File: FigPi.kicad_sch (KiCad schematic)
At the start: 34 parts, among them J1 MOLEX_47346-100147346, J2 Debug, J3 PMW3/PMW4, J4 I2C1/PMW1, J5 SPI0/PWM2/PWM3, J6 I2C0/PMW0, J7 ADC/UART0/UART0/UART1/PWM5/PW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, SW1 KMS233GLFG, SW2 KMS233GLFG, U1 RP2040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

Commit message: Connected USBOOT properly to Boot button.  Had to move capacitor for new track.
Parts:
- U2: value QSPI NOR FLASH 2MiB 2x3mm USON (W25Q16JVUXIM) -> QSPI NOR FLASH 2MiB 2x3mm USON (W25Q16JVUXIQ)
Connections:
- net ~{USB_BOOT}: now also U1.31 (GPIO20)
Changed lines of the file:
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@@
+    (stroke (width 0) (type default) (color 0 0 0 0))
+  )
+  (wire (pts (xy 125.73 213.36) (xy 133.35 213.36))
     (stroke (width 0) (type default) (color 0 0 0 0))
   )
@@
   )
   (label "LED_G" (at 175.26 93.98 0)
+    (effects (font (size 1.27 1.27)) (justify left bottom))
+  )
+  (label "~{USB_BOOT}" (at 127 213.36 0)
     (effects (font (size 1.27 1.27)) (justify left bottom))
   )
@@
       (effects (font (size 1.4986 1.4986)) (justify left bottom))
     )
-    (property "Value" "QSPI NOR FLASH 2MiB 2x3mm USON (W25Q16JVUXIM)" (id 1) (at 227.33 82.55 0)
+    (property "Value" "QSPI NOR FLASH 2MiB 2x3mm USON (W25Q16JVUXIQ)" (id 1) (at 227.33 82.55 0)
       (effects (font (size 1.4986 1.4986)) (justify left bottom))
     )
@@
     )
     (path "/00000000-0000-0000-0000-0000bf9d4e19"
-      (reference "U2") (unit 1) (value "QSPI NOR FLASH 2MiB 2x3mm USON (W25Q16JVUXIM)") (footprint "USON8 2x3")
+      (reference "U2") (unit 1) (value "QSPI NOR FLASH 2MiB 2x3mm USON (W25Q16JVUXIQ)") (footprint "USON8 2x3")
     )
     (path "/c33e8e0a-d848-4eb4-9491-17734fe4442c"

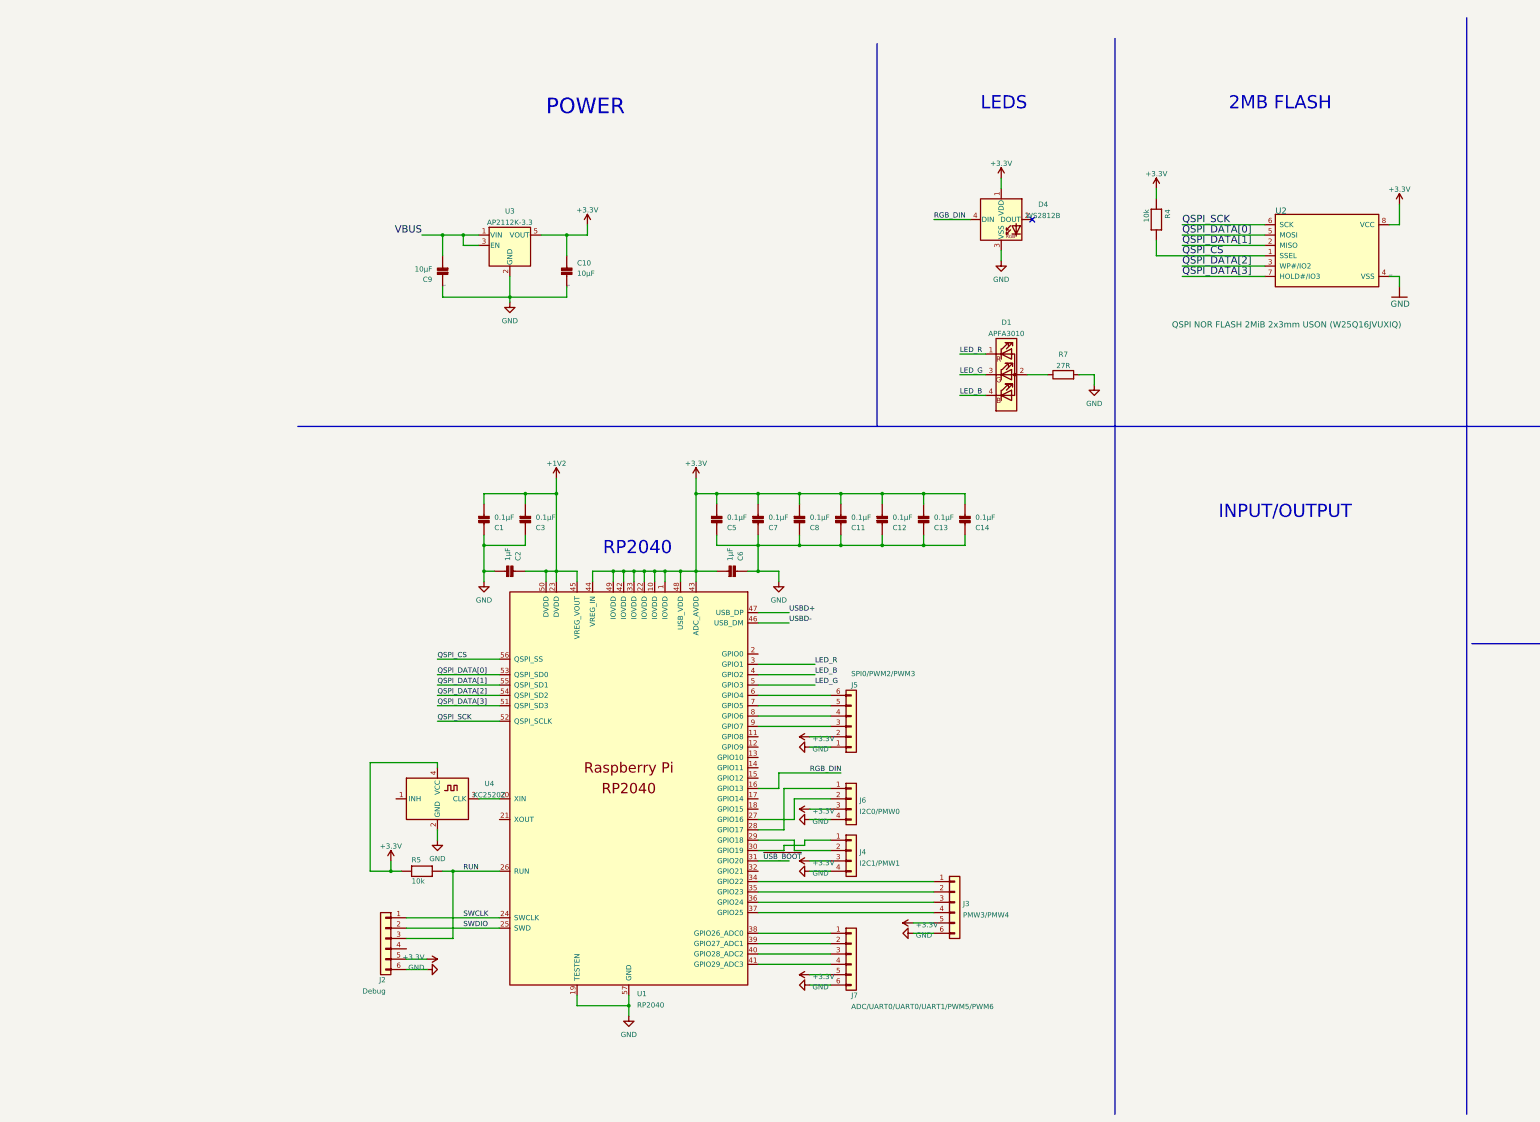
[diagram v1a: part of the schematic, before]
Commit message: v1.5 - Changed all JST connections to 4-pin.  Added 8 additional APA102 - 2020 LEDs for a 3 x 3 matrix.  Rearranged items as needed.  Moved SWDIO and SWCLK from JST connector to test pads.
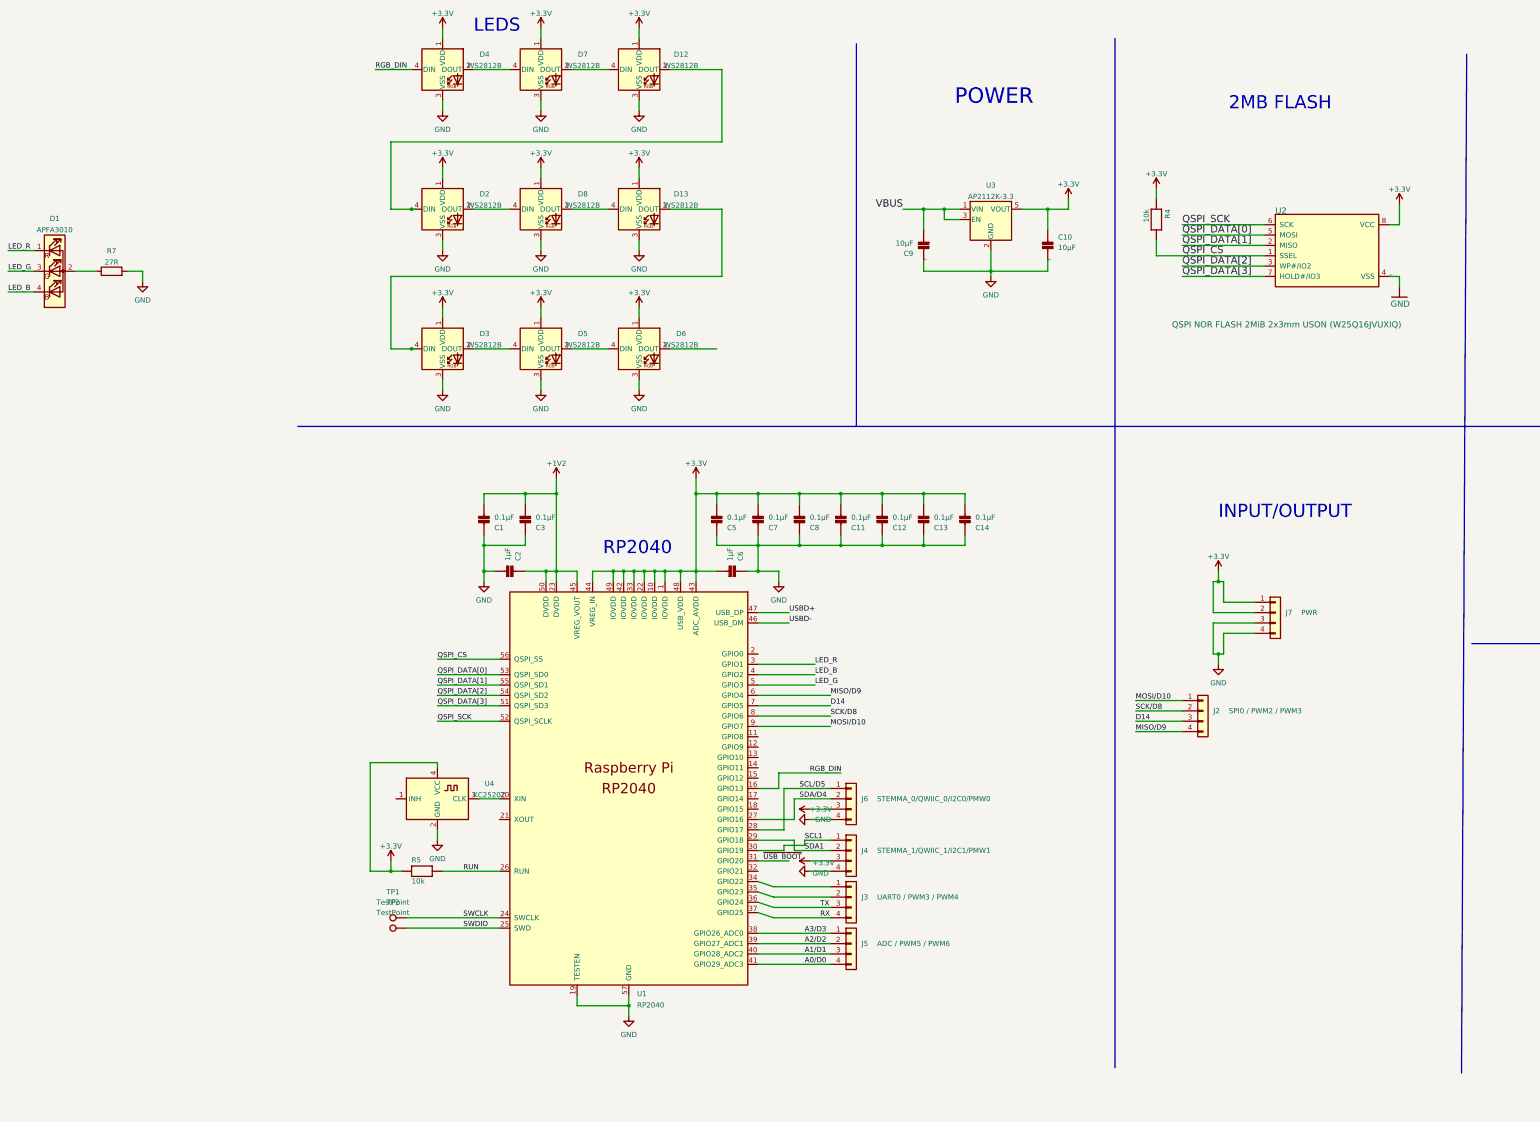
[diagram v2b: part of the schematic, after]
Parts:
- removed J2: Debug, Connector_JST:JST_SH_SM06B-SRSS-TB_1x06-1MP_P1.00mm_Horizontal, symbol Connector_Generic:Conn_01x06
- removed J3: PMW3/PMW4, Connector_JST:JST_SH_SM06B-SRSS-TB_1x06-1MP_P1.00mm_Horizontal, symbol Connector_Generic:Conn_01x06
- removed J5: SPI0/PWM2/PWM3, Connector_JST:JST_SH_SM06B-SRSS-TB_1x06-1MP_P1.00mm_Horizontal, symbol Connector_Generic:Conn_01x06
- removed J7: ADC/UART0/UART0/UART1/PWM5/PWM6, Connector_JST:JST_SH_SM06B-SRSS-TB_1x06-1MP_P1.00mm_Horizontal, symbol Connector_Generic:Conn_01x06
- added D12, D13, D2, D3, D5, D6, D7, D8: WS2812B, LED_SMD:LED_SK6812_EC15_1.5x1.5mm, symbol LED:WS2812B
- added J2: SPI0 / PWM2 / PWM3, Connector_JST:JST_SH_SM04B-SRSS-TB_1x04-1MP_P1.00mm_Horizontal, symbol Connector_Generic:Conn_01x04
- added J3: UART0 / PWM3 / PWM4, Connector_JST:JST_SH_SM04B-SRSS-TB_1x04-1MP_P1.00mm_Horizontal, symbol Connector_Generic:Conn_01x04
- added J5: ADC / PWM5 / PWM6, Connector_JST:JST_SH_SM04B-SRSS-TB_1x04-1MP_P1.00mm_Horizontal, symbol Connector_Generic:Conn_01x04
- added J7: PWR, Connector_JST:JST_SH_SM04B-SRSS-TB_1x04-1MP_P1.00mm_Horizontal, symbol Connector_Generic:Conn_01x04
- added TP1, TP2: TestPoint, TestPoint:TestPoint_Pad_D2.0mm, symbol Connector:TestPoint
- J4: value I2C1/PMW1 -> STEMMA_1/QWIIC_1/I2C1/PMW1
- J6: value I2C0/PMW0 -> STEMMA_0/QWIIC_0/I2C0/PMW0
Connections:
- net +3V3: now also D12.1 (VDD), D13.1 (VDD), D2.1 (VDD), D3.1 (VDD), D5.1 (VDD), D6.1 (VDD), D7.1 (VDD), D8.1 (VDD), J7.1 (Pin_1), J7.2 (Pin_2)
- net GND: now also D12.3 (VSS), D13.3 (VSS), D2.3 (VSS), D3.3 (VSS), D5.3 (VSS), D6.3 (VSS), D7.3 (VSS), D8.3 (VSS), J7.3 (Pin_3), J7.4 (Pin_4)
- net SWCLK: now also TP1.1
- net SWDIO: now also TP2.1
- net at U1.34 (GPIO22): now also J3.1 (Pin_1)
- net at U1.35 (GPIO23): now also J3.2 (Pin_2)
- net TX: now reaches U1.36 (GPIO24)
- net TX: now also J3.3 (Pin_3)
- net RX: now reaches U1.37 (GPIO25)
- net RX: now also J3.4 (Pin_4)
- net A3/D3: now reaches U1.38 (GPIO26_ADC0)
- net A3/D3: now also J5.1 (Pin_1)
- net A2/D2: now reaches U1.39 (GPIO27_ADC1)
- net A2/D2: now also J5.2 (Pin_2)
- net A1/D1: now reaches U1.40 (GPIO28_ADC2)
- net A1/D1: now also J5.3 (Pin_3)
- net A0/D0: now reaches U1.41 (GPIO29_ADC3)
- net A0/D0: now also J5.4 (Pin_4)
- net SCL/D5: now reaches J6.1 (Pin_1), U1.28 (GPIO17)
- net SDA/D4: now reaches J6.2 (Pin_2), U1.27 (GPIO16)
- net at D4.2 (DOUT): now also D7.4 (DIN)
- net MOSI/D10: now reaches U1.9 (GPIO7)
- net MOSI/D10: now also J2.1 (Pin_1)
- net SCK/D8: now reaches U1.8 (GPIO6)
- net SCK/D8: now also J2.2 (Pin_2)
- net D14: now reaches U1.7 (GPIO5)
- net D14: now also J2.3 (Pin_3)
- net MISO/D9: now reaches U1.6 (GPIO4)
- net MISO/D9: now also J2.4 (Pin_4)
- net SCL1: now reaches J4.1 (Pin_1), U1.30 (GPIO19)
- net SDA1: now reaches J4.2 (Pin_2), U1.29 (GPIO18)
- new net: D12.4 (DIN), D7.2 (DOUT)
- new net: D12.2 (DOUT), D2.4 (DIN)
- new net: D3.2 (DOUT), D5.4 (DIN)
- new net: D13.2 (DOUT), D3.4 (DIN)
- new net: D2.2 (DOUT), D8.4 (DIN)
- new net: D5.2 (DOUT), D6.4 (DIN)
- new net: D13.4 (DIN), D8.2 (DOUT)
- no-connect marks 2 -> 1
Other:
- moved on the sheet: C10, C9, D1, D4, R7, U3

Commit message: 1.6 - Minor Cosmetic Changes
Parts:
- TP1, TP2: footprint TestPoint:TestPoint_Pad_D2.0mm -> TestPoint:TestPoint_Pad_D1.0mm
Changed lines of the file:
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@@
     (property "Reference" "TP1" (id 0) (at 36.068 220.98 90))
     (property "Value" "TestPoint" (id 1) (at 36.068 223.52 90))
-    (property "Footprint" "TestPoint:TestPoint_Pad_D2.0mm" (id 2) (at 39.37 222.25 0)
+    (property "Footprint" "TestPoint:TestPoint_Pad_D1.0mm" (id 2) (at 39.37 222.25 0)
       (effects (font (size 1.27 1.27)) hide)
     )
@@
     (property "Reference" "TP2" (id 0) (at 36.068 223.52 90))
     (property "Value" "TestPoint" (id 1) (at 36.068 226.06 90))
-    (property "Footprint" "TestPoint:TestPoint_Pad_D2.0mm" (id 2) (at 39.37 224.79 0)
+    (property "Footprint" "TestPoint:TestPoint_Pad_D1.0mm" (id 2) (at 39.37 224.79 0)
       (effects (font (size 1.27 1.27)) hide)
     )
@@
     )
     (path "/8337b7f2-9099-4db8-9f9b-0f8820b9d737"
-      (reference "TP1") (unit 1) (value "TestPoint") (footprint "TestPoint:TestPoint_Pad_D2.0mm")
+      (reference "TP1") (unit 1) (value "TestPoint") (footprint "TestPoint:TestPoint_Pad_D1.0mm")
     )
     (path "/bf6723a1-f7a8-4f2e-8937-15d1f9150ef9"
-      (reference "TP2") (unit 1) (value "TestPoint") (footprint "TestPoint:TestPoint_Pad_D2.0mm")
+      (reference "TP2") (unit 1) (value "TestPoint") (footprint "TestPoint:TestPoint_Pad_D1.0mm")
     )
     (path "/8642366e-14d5-4a4a-acc5-de8c0e7dc7d5"

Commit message: Updated to Rev 2.1 - layout changes, smd size changes.
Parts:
- removed D1: APFA3010, LED_SMD:LED_Kingbright_APFA3010_3x1.5mm_Horizontal, symbol LED:APFA3010
- added D1: R6C-AM2N2LY, Custom_Library:LED_1.1x1.7mm, symbol Custom_Library:R6C-AM2N2LY
- C1, C11, C12, C13, C14, C3, C5, C6, C7, C8: footprint Capacitor_SMD:C_0603_1608Metric -> Capacitor_SMD:C_0402_1005Metric
- D10: renamed from D6; value WS2812B -> SK6805; footprint LED_SMD:LED_SK6812_EC15_1.5x1.5mm -> Custom_Library:LED_SK6805_EC15_1.5x1.5mm; symbol LED:WS2812B -> Custom_Library:SK6805
- D2: renamed from D4; value WS2812B -> SK6805; footprint LED_SMD:LED_SK6812_EC15_1.5x1.5mm -> Custom_Library:LED_SK6805_EC15_1.5x1.5mm; symbol LED:WS2812B -> Custom_Library:SK6805
- D3: renamed from D2; value WS2812B -> SK6805; footprint LED_SMD:LED_SK6812_EC15_1.5x1.5mm -> Custom_Library:LED_SK6805_EC15_1.5x1.5mm; symbol LED:WS2812B -> Custom_Library:SK6805
- D4: renamed from D3; value WS2812B -> SK6805; footprint LED_SMD:LED_SK6812_EC15_1.5x1.5mm -> Custom_Library:LED_SK6805_EC15_1.5x1.5mm; symbol LED:WS2812B -> Custom_Library:SK6805
- D5: renamed from D7; value WS2812B -> SK6805; footprint LED_SMD:LED_SK6812_EC15_1.5x1.5mm -> Custom_Library:LED_SK6805_EC15_1.5x1.5mm; symbol LED:WS2812B -> Custom_Library:SK6805
- D6: renamed from D8; value WS2812B -> SK6805; footprint LED_SMD:LED_SK6812_EC15_1.5x1.5mm -> Custom_Library:LED_SK6805_EC15_1.5x1.5mm; symbol LED:WS2812B -> Custom_Library:SK6805
- D7: renamed from D5; value WS2812B -> SK6805; footprint LED_SMD:LED_SK6812_EC15_1.5x1.5mm -> Custom_Library:LED_SK6805_EC15_1.5x1.5mm; symbol LED:WS2812B -> Custom_Library:SK6805
- D8: renamed from D12; value WS2812B -> SK6805; footprint LED_SMD:LED_SK6812_EC15_1.5x1.5mm -> Custom_Library:LED_SK6805_EC15_1.5x1.5mm; symbol LED:WS2812B -> Custom_Library:SK6805
- D9: renamed from D13; value WS2812B -> SK6805; footprint LED_SMD:LED_SK6812_EC15_1.5x1.5mm -> Custom_Library:LED_SK6805_EC15_1.5x1.5mm; symbol LED:WS2812B -> Custom_Library:SK6805
- R1, R2: value 27Ω -> 27.4Ω; footprint Resistor_SMD:R_0603_1608Metric -> Resistor_SMD:R_0402_1005Metric
- R3, R4, R5: footprint Resistor_SMD:R_0603_1608Metric -> Resistor_SMD:R_0402_1005Metric
- R7: value 27R -> 260R
- U2: footprint USON8 2x3 -> Custom_Library:USON-8_L3.0-W2.0-P0.50-BL-EP
- U4: value KC2520Z -> OT201612MJBA4SL; footprint Oscillator:Oscillator_SMD_Kyocera_KC2520Z-4Pin_2.5x2.0mm -> Custom_Library:Oscillator_SMD_Yangzing_Tech_SMD2016-4P; JLCPCB P/N (none) -> C669076
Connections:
- net +3V3: now also D10.2 (VDD), D2.2 (VDD), D3.2 (VDD), D4.2 (VDD), D5.2 (VDD), D6.2 (VDD), D7.2 (VDD), D8.2 (VDD), D9.2 (VDD); no longer D10.1 (VDD), D2.1 (VDD), D3.1 (VDD), D4.1 (VDD), D5.1 (VDD), D6.1 (VDD), D7.1 (VDD), D8.1 (VDD), D9.1 (VDD)
- net GND: now also D10.4 (VSS), D2.4 (VSS), D3.4 (VSS), D4.4 (VSS), D5.4 (VSS), D6.4 (VSS), D7.4 (VSS), D8.4 (VSS), D9.4 (VSS); no longer D10.3 (VSS), D2.3 (VSS), D3.3 (VSS), D4.3 (VSS), D5.3 (VSS), D6.3 (VSS), D7.3 (VSS), D8.3 (VSS), D9.3 (VSS)
- net LED_G: now also D1.2 (A)
- net RGB_DIN: now also D2.1 (DIN); no longer D2.4 (DIN)
- net at R7.1: now also D1.1 (C)
- net LED_B: no longer names the net of U1.4 (GPIO2)
- net LED_R: no longer names the net of U1.3 (GPIO1)
- new net: D2.3 (DOUT), D5.1 (DIN)
- new net: D5.3 (DOUT), D8.1 (DIN)
- new net: D3.1 (DIN), D8.3 (DOUT)
- new net: D4.1 (DIN), D9.3 (DOUT)
- new net: D4.3 (DOUT), D7.1 (DIN)
- new net: D3.3 (DOUT), D6.1 (DIN)
- new net: D10.1 (DIN), D7.3 (DOUT)
- new net: D6.3 (DOUT), D9.1 (DIN)
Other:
- moved on the sheet: C1, C11, C12, C13, C14, C2, C3, C5, C6, C7, C8, D10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

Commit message: modified:   FigPi.kicad_pcb modified:   FigPi.kicad_sch
Swapped around the stemma connector pins.
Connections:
- net +3V3: now also J4.2 (Pin_2), J6.2 (Pin_2); no longer J4.3 (Pin_3), J6.3 (Pin_3)
- net GND: now also J4.1 (Pin_1), J6.1 (Pin_1); no longer J4.4 (Pin_4), J6.4 (Pin_4)
- net SCL1: now also J4.4 (Pin_4); no longer J4.1 (Pin_1)
- net SCL/D5: now also J6.4 (Pin_4); no longer J6.1 (Pin_1)
- net SDA1: now also J4.3 (Pin_3); no longer J4.2 (Pin_2)
- net SDA/D4: now also J6.3 (Pin_3); no longer J6.2 (Pin_2)
- net RGB_DIN renamed NEO_DIN
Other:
- moved on the sheet: J3, J4, J6

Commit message: Update to v2.3
Updated the schematic and board to v2.3.
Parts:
- removed J1: MOLEX_47346-100147346, MINI_SAM_D51_r025_b001:MOLEX_47346-1001, symbol MINI_SAM_D51_r025_b001-eagle-import:MOLEX_47346-100147346
- added D11: RB520S-30, Diode_SMD:D_SOD-523, symbol Device:D_Schottky
- added J7: USB_B_Micro, Connector_USB:USB_Micro-B_Molex_47346-0001, symbol Connector:USB_B_Micro
- C1, C3: JLCPCB (none) -> C105882
- C10: renamed from C11; JLCPCB (none) -> C105882
- C11: renamed from C12; JLCPCB (none) -> C105882
- C12: renamed from C13; JLCPCB (none) -> C105882
- C13: renamed from C14; JLCPCB (none) -> C105882
- C2: JLCPCB (none) -> C52923
- C4: renamed from C9; footprint MINI_SAM_D51_r025_b001:0603_CAPACITOR -> Resistor_SMD:R_0603_1608Metric; JLCPCB (none) -> C85713
- C5: renamed from C10; footprint MINI_SAM_D51_r025_b001:0603_CAPACITOR -> Resistor_SMD:R_0603_1608Metric; JLCPCB (none) -> C85713
- C6: renamed from C5; JLCPCB (none) -> C105882
- C7: renamed from C6; JLCPCB (none) -> C52923
- C8: renamed from C7; JLCPCB (none) -> C105882
- C9: renamed from C8; JLCPCB (none) -> C105882
- D1: renamed from D2; JLCPCB (none) -> C2890035
- D10: renamed from D1; JLCPCB (none) -> C605457
- D2: renamed from D5; JLCPCB (none) -> C2890035
- D3: renamed from D8; JLCPCB (none) -> C2890035
- D4: renamed from D3; JLCPCB (none) -> C2890035
- D5: renamed from D6; JLCPCB (none) -> C2890035
- D6: renamed from D9; JLCPCB (none) -> C2890035
- D7: renamed from D4; JLCPCB (none) -> C2890035
- D8: renamed from D7; JLCPCB (none) -> C2890035
- D9: renamed from D10; JLCPCB (none) -> C2890035
- J1: renamed from J7; JLCPCB (none) -> C160404
- J2, J4: JLCPCB (none) -> C160404
- J3: renamed from J6; JLCPCB (none) -> C160404
- J5: renamed from J3; JLCPCB (none) -> C160404
- J6: renamed from J5; JLCPCB (none) -> C160404
- R1: renamed from R7; JLCPCB (none) -> C227740
- R2: renamed from R5; symbol MINI_SAM_D51_r025_b001-eagle-import:RESISTORQUIRKY -> Device:R_Small; JLCPCB (none) -> C144731
- R3: renamed from R4; symbol MINI_SAM_D51_r025_b001-eagle-import:RESISTORQUIRKY -> Device:R_Small; JLCPCB (none) -> C144731
- R4: renamed from R2; symbol MINI_SAM_D51_r025_b001-eagle-import:RESISTORQUIRKY -> Device:R_Small; JLCPCB (none) -> C274349
- R5: renamed from R1; symbol MINI_SAM_D51_r025_b001-eagle-import:RESISTORQUIRKY -> Device:R_Small; JLCPCB (none) -> C274349
- R6: renamed from R3; symbol MINI_SAM_D51_r025_b001-eagle-import:RESISTORQUIRKY -> Device:R_Small; JLCPCB (none) -> C105637
- SW1, SW2: value KMS233GLFG -> KMS231GLFG; JLCPCB (none) -> C221701
- U1: JLCPCB (none) -> C2040
- U2: value QSPI NOR FLASH 2MiB 2x3mm USON (W25Q16JVUXIQ) -> QSPI NOR FLASH 2MiB 2x3mm USON (W25Q16JVUXxQ); JLCPCB (none) -> C2843335
- U3: renamed from U4; JLCPCB (none) -> C669076
- U4: renamed from U3; JLCPCB (none) -> C3021085; JLCPCB P/N (none) -> C3021085
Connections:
- net D14: now also J2.2 (Pin_2); no longer J2.3 (Pin_3)
- net GND: now also SW1.1, SW1.5, J7.5 (GND), J7.6 (Shield); no longer SW1.2, SW1.3, SW1.4
- net MISO/D9: now also J2.1 (Pin_1); no longer J2.4 (Pin_4)
- net MOSI/D10: now also J2.4 (Pin_4); no longer J2.1 (Pin_1)
- net SCK/D8: now also J2.3 (Pin_3); no longer J2.2 (Pin_2)
- net VBUS: now also J7.1 (VBUS)
- net at R4.2: now also J7.2 (D-)
- net at R5.2: now also J7.3 (D+)
- net LED: now reaches U1.2 (GPIO0)
- net LED: now also D10.2 (A)
- net +3V3 renamed +3.3V
- net +3.3V: now also R2.2; no longer R2.1
- net LED_G: no longer names the net of U1.5 (GPIO3)
- net LED_G: no longer D10.2 (A)
- net QSPI_DATA[0] renamed QSPI_SD0
- net QSPI_DATA[1] renamed QSPI_SD1
- net QSPI_DATA[2] renamed QSPI_SD2
- net QSPI_DATA[3] renamed QSPI_SD3
- removed net RUN: R2.2, SW1.1, SW1.5, U1.26 (RUN)
- net ~{USB_BOOT} renamed BUTTON
- net BUTTON: now also D11.1 (K); no longer R6.1
- new net: D11.2 (A), R6.1
- new net ~{RESET}: R2.1, SW1.2, SW1.3, SW1.4, U1.26 (RUN)
- no-connect marks 1 -> 15
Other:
- note added: "REAR LED"
- note removed: "INPUT/OUTPUT"
- note removed: "MOLEX 47346-1001"
- company: (none) -> Benjamin Shockley
- title: Mini SAM D51 -> Fig Pi
- moved on the sheet: C1, C10, C11, C12, C13, C2, C3, C4, C5, C6, C7, C8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
